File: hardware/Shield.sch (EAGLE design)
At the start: 25 parts, among them J1 AVR_SPI_PRG_6PTH, Q8 TIP120, U2 LM78XX-TO252-3, U4 ATMEGA328P_PDIP, Y1 16Mhz

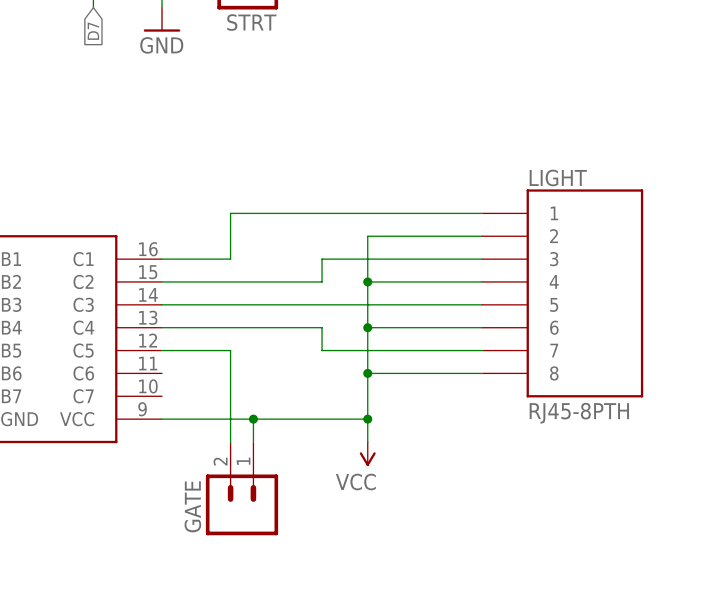
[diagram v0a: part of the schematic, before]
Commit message: Switched wiring for lights to clean up board layout
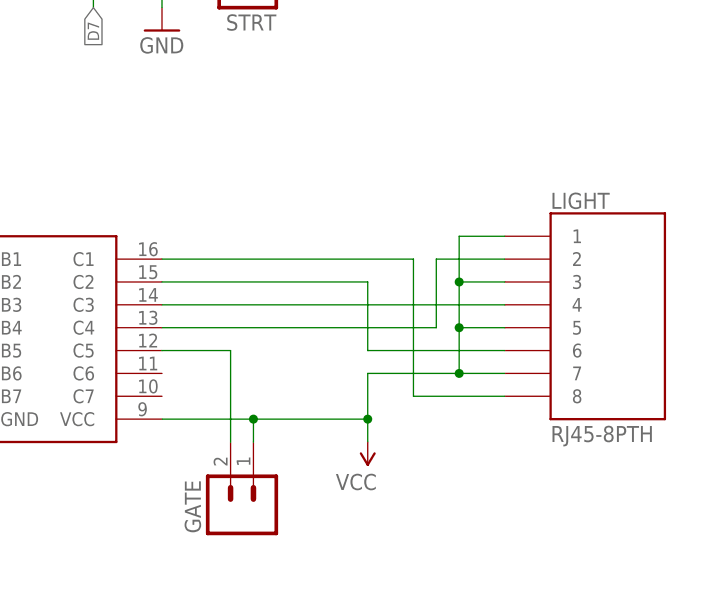
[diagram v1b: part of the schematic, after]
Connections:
- net N$2: now also LIGHT.8; no longer LIGHT.1
- net N$3: now also LIGHT.6; no longer LIGHT.3
- net N$4: now also LIGHT.4; no longer LIGHT.5
- net N$5: now also LIGHT.2; no longer LIGHT.7
- net VCC: now also LIGHT.1, LIGHT.3, LIGHT.5, LIGHT.7; no longer LIGHT.2, LIGHT.4, LIGHT.6, LIGHT.8
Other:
- moved on the sheet: LIGHT
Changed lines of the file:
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@@
 <instance part="GND1" gate="1" x="-27.94" y="22.86" rot="R270"/>
 <instance part="R7" gate="G$1" x="-15.24" y="30.48" rot="R180"/>
-<instance part="LIGHT" gate="G$1" x="50.8" y="76.2"/>
+<instance part="LIGHT" gate="G$1" x="53.34" y="73.66"/>
 <instance part="GATE" gate="G$1" x="12.7" y="53.34" rot="R90"/>
 <instance part="PWR" gate="G$1" x="-109.22" y="111.76" rot="R180"/>
@@
 </segment>
 <segment>
-<wire x1="25.4" y1="83.82" x2="25.4" y2="78.74" width="0.1524" layer="91"/>
-<wire x1="25.4" y1="78.74" x2="25.4" y2="73.66" width="0.1524" layer="91"/>
-<wire x1="25.4" y1="73.66" x2="25.4" y2="68.58" width="0.1524" layer="91"/>
-<wire x1="25.4" y1="68.58" x2="38.1" y2="68.58" width="0.1524" layer="91"/>
-<wire x1="38.1" y1="73.66" x2="25.4" y2="73.66" width="0.1524" layer="91"/>
-<junction x="25.4" y="73.66"/>
-<wire x1="38.1" y1="78.74" x2="25.4" y2="78.74" width="0.1524" layer="91"/>
-<junction x="25.4" y="78.74"/>
-<wire x1="38.1" y1="83.82" x2="25.4" y2="83.82" width="0.1524" layer="91"/>
-<junction x="25.4" y="68.58"/>
-<wire x1="25.4" y1="68.58" x2="25.4" y2="63.5" width="0.1524" layer="91"/>
-<pinref part="LIGHT" gate="G$1" pin="2"/>
-<pinref part="LIGHT" gate="G$1" pin="4"/>
-<pinref part="LIGHT" gate="G$1" pin="8"/>
-<pinref part="LIGHT" gate="G$1" pin="6"/>
 <pinref part="VCC_PWR4" gate="1" pin="VCC"/>
 <pinref part="U$1" gate="G$1" pin="VCC"/>
 <wire x1="25.4" y1="63.5" x2="25.4" y2="60.96" width="0.1524" layer="91"/>
 <wire x1="2.54" y1="63.5" x2="12.7" y2="63.5" width="0.1524" layer="91"/>
-<junction x="25.4" y="63.5"/>
 <pinref part="GATE" gate="G$1" pin="1"/>
 <wire x1="12.7" y1="63.5" x2="25.4" y2="63.5" width="0.1524" layer="91"/>
 <wire x1="12.7" y1="63.5" x2="12.7" y2="60.96" width="0.1524" layer="91"/>
 <junction x="12.7" y="63.5"/>
+<pinref part="LIGHT" gate="G$1" pin="7"/>
+<wire x1="40.64" y1="68.58" x2="35.56" y2="68.58" width="0.1524" layer="91"/>
+<wire x1="35.56" y1="68.58" x2="25.4" y2="68.58" width="0.1524" layer="91"/>
+<wire x1="25.4" y1="68.58" x2="25.4" y2="63.5" width="0.1524" layer="91"/>
+<wire x1="35.56" y1="68.58" x2="35.56" y2="73.66" width="0.1524" layer="91"/>
+<wire x1="35.56" y1="73.66" x2="35.56" y2="78.74" width="0.1524" layer="91"/>
+<pinref part="LIGHT" gate="G$1" pin="5"/>
+<wire x1="40.64" y1="73.66" x2="35.56" y2="73.66" width="0.1524" layer="91"/>
+<pinref part="LIGHT" gate="G$1" pin="3"/>
+<wire x1="40.64" y1="78.74" x2="35.56" y2="78.74" width="0.1524" layer="91"/>
+<junction x="35.56" y="73.66"/>
+<junction x="35.56" y="68.58"/>
+<pinref part="LIGHT" gate="G$1" pin="1"/>
+<wire x1="40.64" y1="83.82" x2="35.56" y2="83.82" width="0.1524" layer="91"/>
+<wire x1="35.56" y1="83.82" x2="35.56" y2="78.74" width="0.1524" layer="91"/>
+<junction x="35.56" y="78.74"/>
+<junction x="25.4" y="63.5"/>
 </segment>
 <segment>
@@
 <segment>
 <pinref part="U$1" gate="G$1" pin="C1"/>
-<wire x1="2.54" y1="81.28" x2="10.16" y2="81.28" width="0.1524" layer="91"/>
-<wire x1="10.16" y1="81.28" x2="10.16" y2="86.36" width="0.1524" layer="91"/>
-<pinref part="LIGHT" gate="G$1" pin="1"/>
-<wire x1="10.16" y1="86.36" x2="38.1" y2="86.36" width="0.1524" layer="91"/>
+<wire x1="2.54" y1="81.28" x2="30.48" y2="81.28" width="0.1524" layer="91"/>
+<wire x1="30.48" y1="81.28" x2="30.48" y2="66.04" width="0.1524" layer="91"/>
+<pinref part="LIGHT" gate="G$1" pin="8"/>
+<wire x1="30.48" y1="66.04" x2="40.64" y2="66.04" width="0.1524" layer="91"/>
 </segment>
 </net>
@@
 <segment>
 <pinref part="U$1" gate="G$1" pin="C2"/>
-<wire x1="2.54" y1="78.74" x2="20.32" y2="78.74" width="0.1524" layer="91"/>
-<wire x1="20.32" y1="78.74" x2="20.32" y2="81.28" width="0.1524" layer="91"/>
-<pinref part="LIGHT" gate="G$1" pin="3"/>
-<wire x1="20.32" y1="81.28" x2="38.1" y2="81.28" width="0.1524" layer="91"/>
+<wire x1="2.54" y1="78.74" x2="25.4" y2="78.74" width="0.1524" layer="91"/>
+<wire x1="25.4" y1="78.74" x2="25.4" y2="71.12" width="0.1524" layer="91"/>
+<pinref part="LIGHT" gate="G$1" pin="6"/>
+<wire x1="25.4" y1="71.12" x2="40.64" y2="71.12" width="0.1524" layer="91"/>
+</segment>
+</net>
+<net name="N$5" class="0">
+<segment>
+<pinref part="U$1" gate="G$1" pin="C4"/>
+<wire x1="33.02" y1="73.66" x2="2.54" y2="73.66" width="0.1524" layer="91"/>
+<pinref part="LIGHT" gate="G$1" pin="2"/>
+<wire x1="40.64" y1="81.28" x2="33.02" y2="81.28" width="0.1524" layer="91"/>
+<wire x1="33.02" y1="81.28" x2="33.02" y2="73.66" width="0.1524" layer="91"/>
 </segment>
 </net>
@@
 <segment>
 <pinref part="U$1" gate="G$1" pin="C3"/>
-<pinref part="LIGHT" gate="G$1" pin="5"/>
-<wire x1="2.54" y1="76.2" x2="38.1" y2="76.2" width="0.1524" layer="91"/>
-</segment>
-</net>
-<net name="N$5" class="0">
-<segment>
-<pinref part="LIGHT" gate="G$1" pin="7"/>
-<wire x1="38.1" y1="71.12" x2="20.32" y2="71.12" width="0.1524" layer="91"/>
-<wire x1="20.32" y1="71.12" x2="20.32" y2="73.66" width="0.1524" layer="91"/>
-<pinref part="U$1" gate="G$1" pin="C4"/>
-<wire x1="20.32" y1="73.66" x2="2.54" y2="73.66" width="0.1524" layer="91"/>
-</segment>
-</net>
+<wire x1="2.54" y1="76.2" x2="40.64" y2="76.2" width="0.1524" layer="91"/>
+<pinref part="LIGHT" gate="G$1" pin="4"/>
+</segment>
+</net>
